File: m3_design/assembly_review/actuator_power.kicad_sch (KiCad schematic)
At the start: 15 parts, among them Q120 AONR21357, Q121 AONR21357, Q122 AO3400A

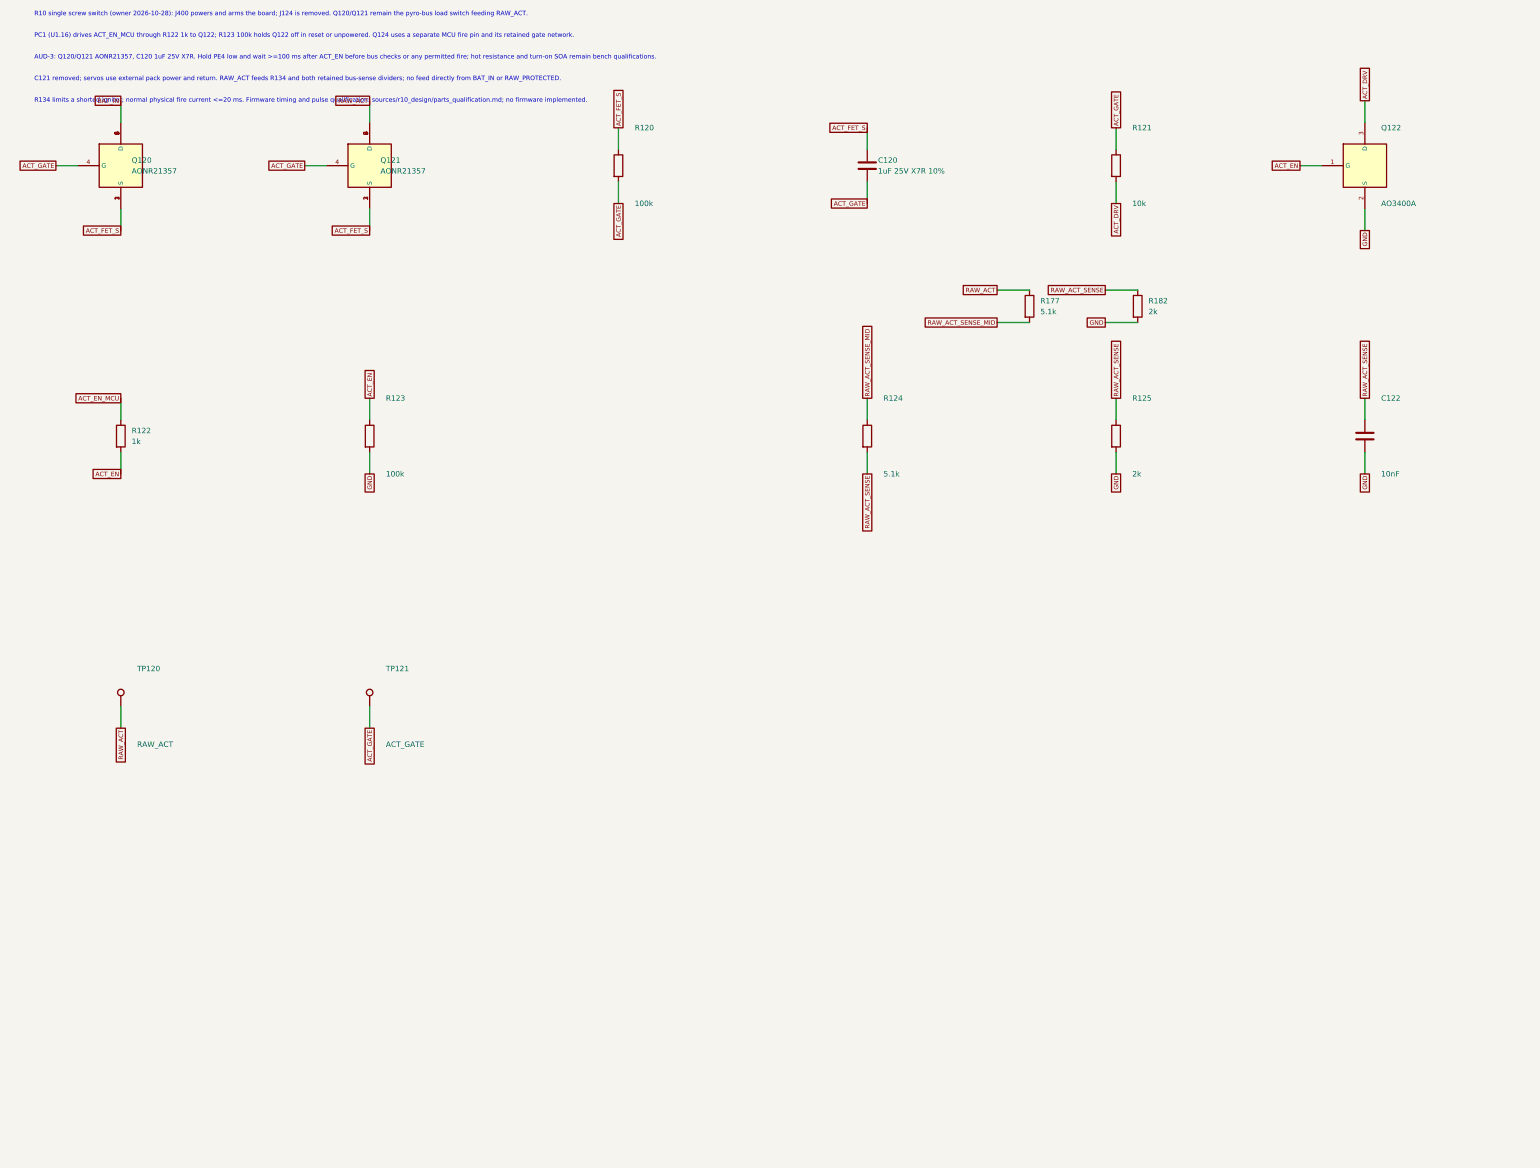
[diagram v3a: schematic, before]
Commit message: Finish R10 round 9 Minor fix pass
Complete the interrupted generator rebuild and apply the recorded round 9
Minor fixes: capacitor labels, cold-screen ordering, debugger instructions,
local route cleanups, gate fault detection and explicit R10 procurement limits.
Refresh the board-bound fabrication, supplier and validation records.

Round 9 reviewed 8bccb07: 0 Critical, 0 Major, 21 Minor groups. Round 10 will
freshly review this committed fix pass, including every changed CAD item.

Board SHA-256: b337fe63c258c85ba4120e75ad018afa0c22241f8bc21a4172787cf2887208d9
Board: 46 x 90 mm, 2366509 bytes. Two COMPLETE builds pass; all 21 generated
CAD and binding files are byte-identical.

Unskipped tools/check.sh: exit 0.
DRC violations 0; unconnected 0; schematic parity 0; ERC 0.
Metadata / 3D, silk, fit / plate, all 33 R10 rules, routing hygiene, actuator
contract and current 5-output fabrication manifest: OK.
Self-tests: shell 4, procurement 19, fit 24, paste 5, routing 59, R10 140;
3 NumPy cases rerun successfully, no unresolved skips. Hot-plug: 2304/2304
required cases pass (simulation / Inference).

Fab export, required fitting, orientation and paste pass: 215 CPL rows,
82 BOM codes. Fresh supplier/procurement checks correctly FAIL the known
$84.43 versus $84.41 cap and R430/U4 stock shortages; 46 Extended codes.
OQ-3 and final deviation acceptance remain pending. No firmware, bench,
installed RF immunity, physical fit, assembly-process or flight result claimed.

Evidence: docs/R10_VALIDATION.md and sources/r10_review/round9_fix_validation.json
and round9_fix_check.txt under m3_design/assembly_review. Native headless
KiCad environment uses the external D-R1-05 mouse-query workaround only;
repository gates and CAD rules are unchanged by that workaround.

Co-Authored-By: Claude Opus 5.5 <noreply@anthropic.com>
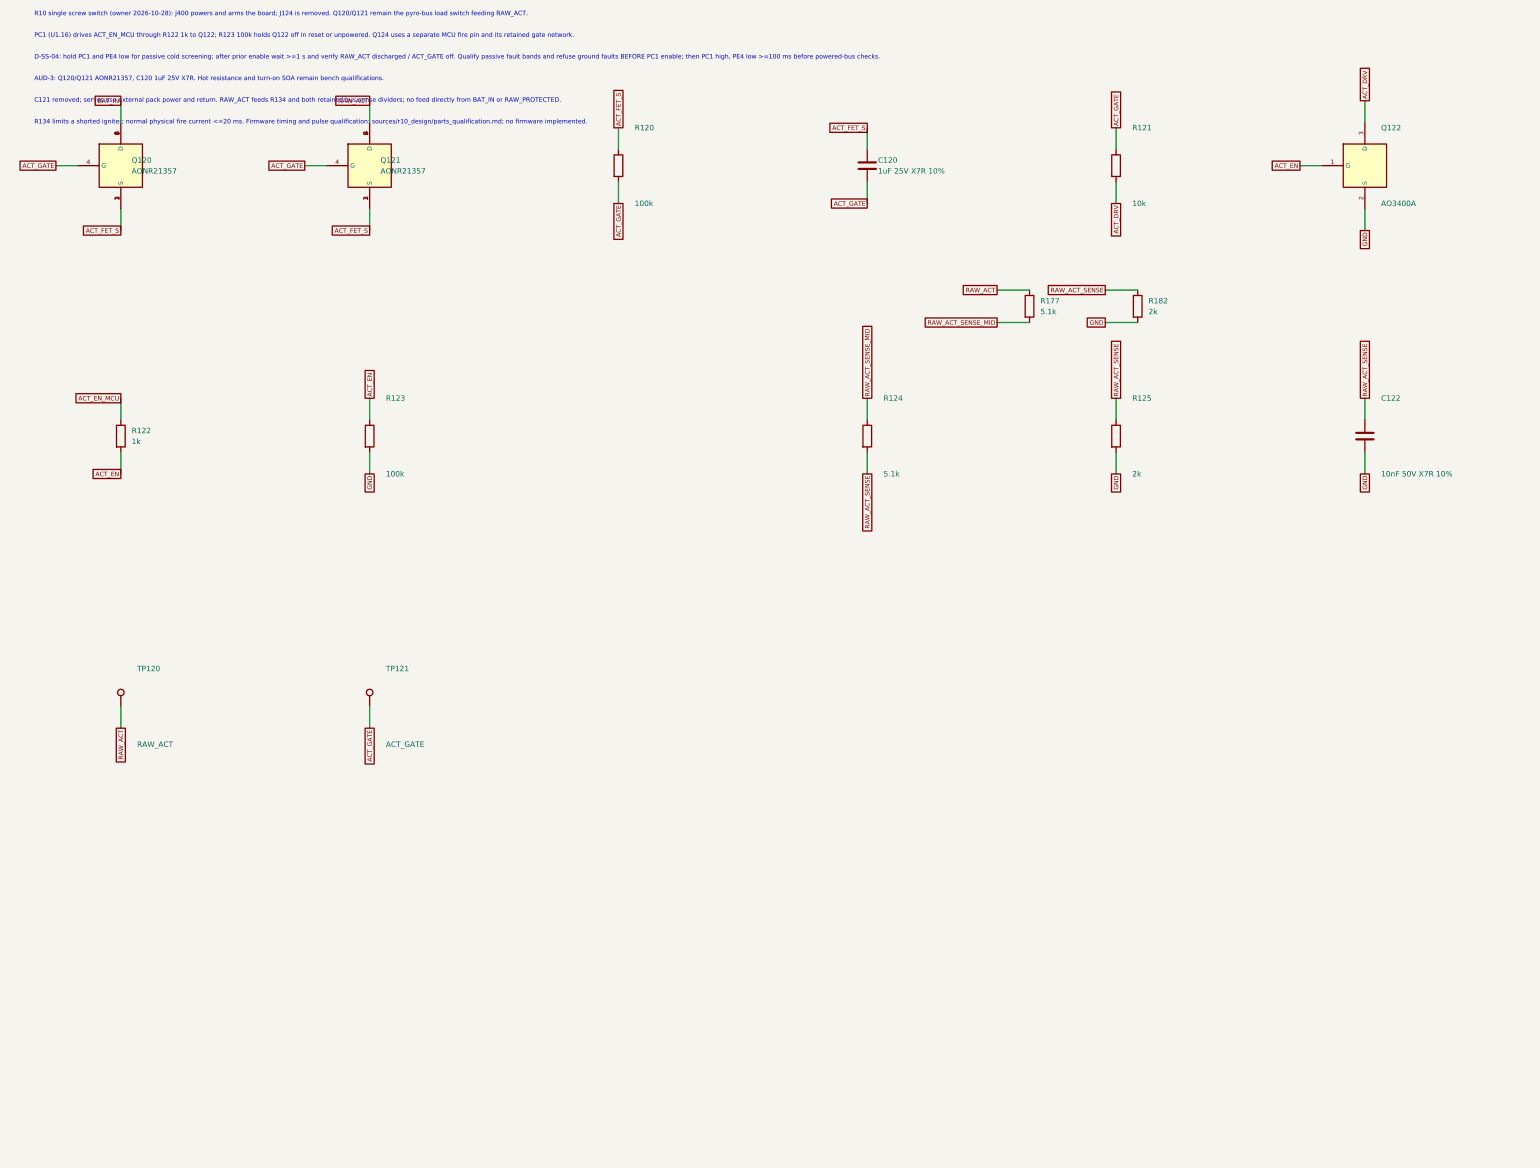
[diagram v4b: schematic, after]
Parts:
- C122: value 10nF -> 10nF 50V X7R 10%
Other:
- note added: "AUD-3: Q120/Q121 AONR21357, C120 1uF 25V X7R. Hot resistance and turn-on SOA remain bench qualifications."
- note added: "D-SS-04: hold PC1 and PE4 low for passive cold screening; after prior enable wait >=1 s and verify RAW_ACT discharged / ACT_GATE off. Qualify passive fault bands and refuse ground faults BEFORE PC1 enable; then PC1 high, PE4 low >=100 ms before powered-bus checks."
- note removed: "AUD-3: Q120/Q121 AONR21357, C120 1uF 25V X7R. Hold PE4 low and wait >=100 ms after ACT_EN before bus checks or any permitted fire; hot resistance and turn-on SOA remain bench qualifications."
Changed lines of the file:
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@@
 					(size 1.27 1.27))
 				(justify left)))
-		(property "Value" "10nF"
+		(property "Value" "10nF 50V X7R 10%"
 			(at 336.55 123.19 0)
 			(effects
@@
 			(justify left))
 )
-	(text "AUD-3: Q120/Q121 AONR21357, C120 1uF 25V X7R. Hold PE4 low and wait >=100 ms after ACT_EN before bus checks or any permitted fire; hot resistance and turn-on SOA remain bench qualifications."
+	(text "D-SS-04: hold PC1 and PE4 low for passive cold screening; after prior enable wait >=1 s and verify RAW_ACT discharged / ACT_GATE off. Qualify passive fault bands and refuse ground faults BEFORE PC1 enable; then PC1 high, PE4 low >=100 ms before powered-bus checks."
 		(at 20.32 25.4 0)
 		(effects
@@
 			(justify left))
 )
+	(text "AUD-3: Q120/Q121 AONR21357, C120 1uF 25V X7R. Hot resistance and turn-on SOA remain bench qualifications."
+		(at 20.32 30.48 0)
+		(effects
+			(font
+				(size 1.05 1.05))
+			(justify left))
+)
 	(text "C121 removed; servos use external pack power and return. RAW_ACT feeds R134 and both retained bus-sense dividers; no feed directly from BAT_IN or RAW_PROTECTED."
-		(at 20.32 30.48 0)
+		(at 20.32 35.56 0)
 		(effects
 			(font
@@
 )
 	(text "R134 limits a shorted igniter; normal physical fire current <=20 ms. Firmware timing and pulse qualification: sources/r10_design/parts_qualification.md; no firmware implemented."
-		(at 20.32 35.56 0)
-		(effects
-			(font
+		(at 20.32 40.64 0)
+		(effects
+			(font
